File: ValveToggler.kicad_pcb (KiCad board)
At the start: 2 copper layers, 70 x 50 mm, 29 parts, among them J1 24V IN, J17 MODE, J2 Coil1, J3 Coil2, Q6 BC557, Q7 2N7000, Q8 BC557, Q9 2N7000, U1 NE555P, U2 NE555P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

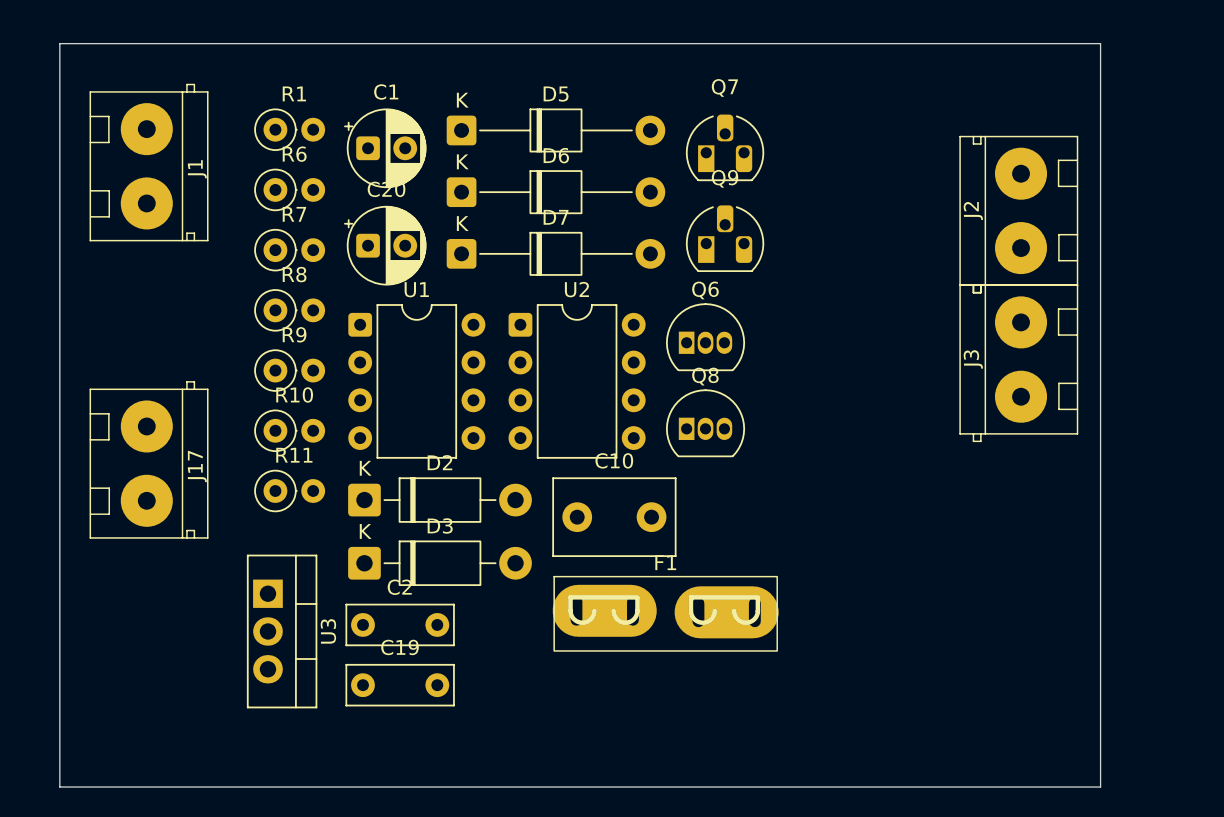
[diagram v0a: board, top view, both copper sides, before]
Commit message: Layout: Arrange footprints, start poc routing
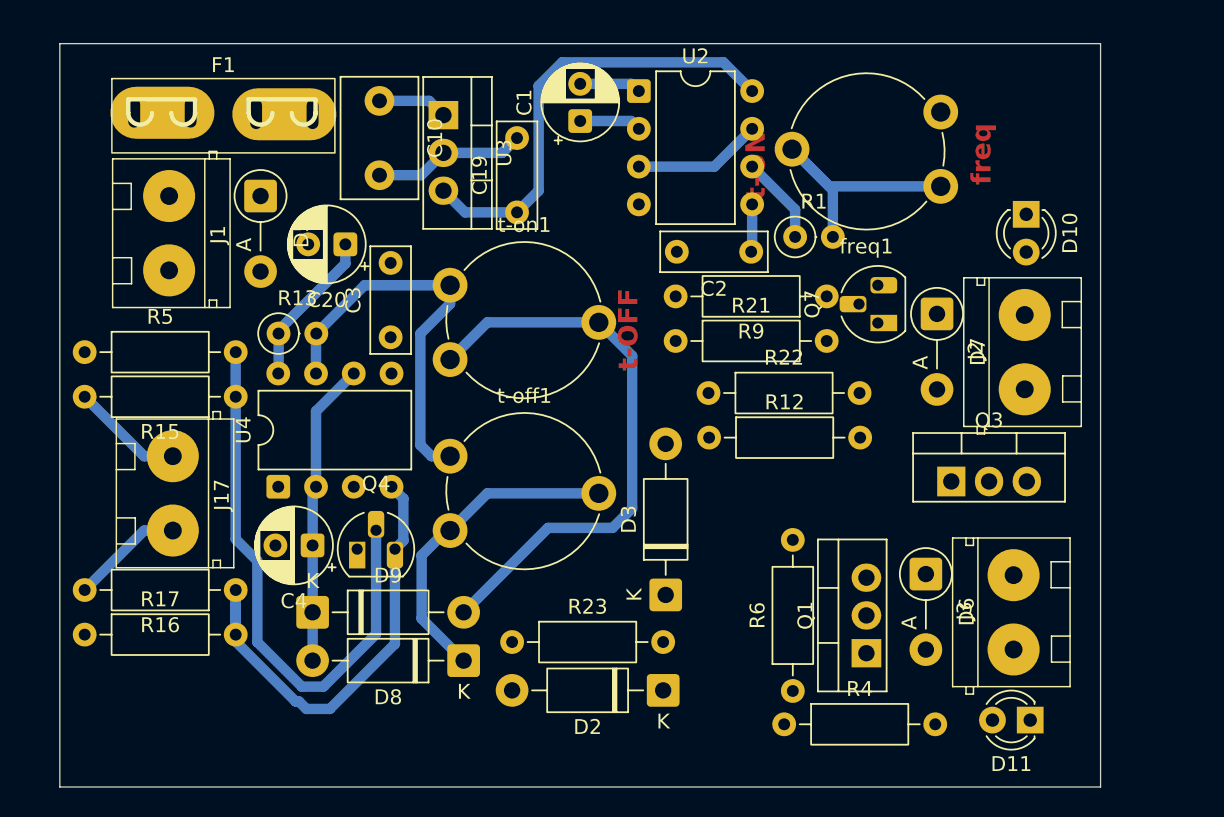
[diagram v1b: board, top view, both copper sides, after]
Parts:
- removed Q6, Q8: BC557, Package_TO_SOT_THT:TO-92_Inline
- removed Q9: 2N7000, Package_TO_SOT_THT:TO-92_HandSolder
- removed R10: 10k, Resistor_THT:R_Axial_DIN0207_L6.3mm_D2.5mm_P2.54mm_Vertical
- removed R11, R7, R8: 47k, Resistor_THT:R_Axial_DIN0207_L6.3mm_D2.5mm_P2.54mm_Vertical
- removed U1: NE555P, Package_DIP:DIP-8_W7.62mm
- added C3: 100nF, Capacitor_THT:C_Disc_D7.0mm_W2.5mm_P5.00mm, F.Cu at (67.2, 64.8)
- added C4: 47u, Capacitor_THT:CP_Radial_D5.0mm_P2.50mm, F.Cu at (62.0, 78.8)
- added D10: LED2_orange, LED_THT:LED_D3.0mm_Clear, F.Cu at (110.0, 56.5)
- added D11: LED1_green, LED_THT:LED_D3.0mm_Clear, F.Cu at (110.3, 90.5)
- added D8: 1N5817, Diode_THT:D_DO-41_SOD81_P10.16mm_Horizontal, F.Cu at (72.2, 86.5)
- added D9: 1N5817, Diode_THT:D_DO-41_SOD81_P10.16mm_Horizontal, F.Cu at (62.0, 83.2)
- added Q1: IRFZ24N, Package_TO_SOT_THT:TO-220-3_Vertical, F.Cu at (99.2, 86.0)
- added Q3: IRFZ24N, Package_TO_SOT_THT:TO-220-3_Vertical, F.Cu at (105.0, 74.5)
- added Q4: 2N7000, Package_TO_SOT_THT:TO-92_HandSolder, F.Cu at (65.0, 79.0)
- added R12: 1k5, Resistor_THT:R_Axial_DIN0207_L6.3mm_D2.5mm_P10.16mm_Horizontal, F.Cu at (88.7, 71.5)
- added R13: 1k5, Resistor_THT:R_Axial_DIN0207_L6.3mm_D2.5mm_P2.54mm_Vertical, F.Cu at (59.7, 64.5)
- added R15: 2k2, Resistor_THT:R_Axial_DIN0207_L6.3mm_D2.5mm_P10.16mm_Horizontal, F.Cu at (56.8, 68.8)
- added R16: 2k2, Resistor_THT:R_Axial_DIN0207_L6.3mm_D2.5mm_P10.16mm_Horizontal, F.Cu at (56.8, 81.8)
- added R17: 2k2, Resistor_THT:R_Axial_DIN0207_L6.3mm_D2.5mm_P10.16mm_Horizontal, F.Cu at (46.7, 84.8)
- added R21: 330, Resistor_THT:R_Axial_DIN0207_L6.3mm_D2.5mm_P10.16mm_Horizontal, F.Cu at (86.4, 65.0)
- added R22: 330, Resistor_THT:R_Axial_DIN0207_L6.3mm_D2.5mm_P10.16mm_Horizontal, F.Cu at (88.6, 68.5)
- added R23: 330, Resistor_THT:R_Axial_DIN0207_L6.3mm_D2.5mm_P10.16mm_Horizontal, F.Cu at (75.4, 85.2)
- added R4: 1k5, Resistor_THT:R_Axial_DIN0207_L6.3mm_D2.5mm_P10.16mm_Horizontal, F.Cu at (93.7, 90.8)
- added R5: 2k2, Resistor_THT:R_Axial_DIN0207_L6.3mm_D2.5mm_P10.16mm_Horizontal, F.Cu at (46.7, 65.8)
- added U4: NE555P, Package_DIP:DIP-8_W7.62mm, F.Cu at (59.7, 74.8)
- added freq1: 10k, Potentiometer_THT:Potentiometer_Piher_PT-10-V10_Vertical, F.Cu at (104.2, 49.6)
- added t-off1: 100k, Potentiometer_THT:Potentiometer_Piher_PT-10-V10_Vertical, F.Cu at (71.2, 77.8)
- added t-on1: 10k, Potentiometer_THT:Potentiometer_Piher_PT-10-V10_Vertical, F.Cu at (71.2, 66.2)
- D5, D6, D7: footprint Diode_THT:D_T-1_P12.70mm_Horizontal -> Diode_THT:D_DO-41_SOD81_P5.08mm_Vertical_AnodeUp
- J17: value MODE -> MODE (24V)
- J2: value Coil1 -> Coil2
- J3: value Coil2 -> Coil1
- R1: value 10k -> 1k5
- R6: value 47k -> 10k; footprint Resistor_THT:R_Axial_DIN0207_L6.3mm_D2.5mm_P2.54mm_Vertical -> Resistor_THT:R_Axial_DIN0207_L6.3mm_D2.5mm_P10.16mm_Horizontal
- R9: footprint Resistor_THT:R_Axial_DIN0207_L6.3mm_D2.5mm_P2.54mm_Vertical -> Resistor_THT:R_Axial_DIN0207_L6.3mm_D2.5mm_P10.16mm_Horizontal
- moved R6 48.4 mm to (94.3, 88.5), turned to 90 degrees
- moved F1 44.8 mm to (50.0, 49.8)
- moved D6 40.4 mm to (103.2, 80.7), turned to -90 degrees
- moved R9 37.4 mm to (96.6, 62.0), turned to 180 degrees
- moved C2 36.2 mm to (91.5, 59.0), turned to 180 degrees
- moved R1 35.7 mm to (94.5, 58.0)
- moved U3 34.3 mm to (70.8, 49.8)
- moved C19 33.4 mm to (75.8, 56.4), turned to 90 degrees
- moved D7 32.2 mm to (104.0, 63.2), turned to -90 degrees
- moved C10 31.0 mm to (66.5, 48.9), turned to -90 degrees
- moved D2 23.8 mm to (85.6, 88.5), turned to 180 degrees
- moved D3 20.4 mm to (85.8, 82.1), turned to 90 degrees
- moved U2 17.6 mm to (83.9, 48.2)
- moved J3 17.0 mm to (109.2, 85.8)
- moved Q7 16.3 mm to (100.0, 63.8), turned to 90 degrees
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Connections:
- net Net-(Q4-G) renamed /MOS2
- C10 pad 2: GNDPWR -> GND
- C19 pad 1: +5VA -> +12V
- C19 pad 2: GNDPWR -> GND
- C20 pad 1: +5VA -> +12V
- C20 pad 2: GNDPWR -> GND
- D2 pad 1: Net-(D2-K) -> /MOS1
- D2 pad 2: /F1 -> /F1_signal-mode1
- D3 pad 1: Net-(D2-K) -> /MOS1
- D3 pad 2: /F2 -> /F2_signal-mode2
- D5 pad 2: GNDPWR -> GND
- J1 pad 2: GNDPWR -> GND
- J17 pad 1: /MODE_SINGLE -> /MODE_DOUBLE_IN
- J17 pad 2: /MODE_DOUBLE -> /MODE_SINGLE_IN
- Q7 pad 2: /F2 -> Net-(Q7-G)
- R1 pad 2: /F2 -> Net-(R1-Pad2)
- R6 pad 1: Net-(D2-K) -> Net-(Q1-G)
- R6 pad 2: GNDPWR -> GND
- R9 pad 2: Net-(Q8-C) -> /MODE_DOUBLE_12V
- U2 pad 3: /F2 -> /F2_signal-mode2
- U2 pad 4: /MODE_DOUBLE -> /MODE_DOUBLE_12V
- U2 pad 7: /F2 -> /F2_signal-mode2
- U3 pad 2: GNDPWR -> GND
- U3 pad 3: +5VA -> +12V
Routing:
- net +12V: track 0.00 -> 41.0 mm
- net Net-(D9-A): track 0.00 -> 38.7 mm
- net /MODE_DOUBLE_12V: track 0.00 -> 37.8 mm
- net /MODE_SINGLE_12V: track 0.00 -> 32.0 mm
- net Net-(U4-DIS): track 0.00 -> 26.9 mm
- net Net-(D8-K): track 0.00 -> 21.9 mm
- net Net-(D8-A): track 0.00 -> 20.5 mm
- net Net-(R1-Pad2): track 0.00 -> 18.1 mm
- net GND: track 0.00 -> 14.4 mm
- net Net-(U2-THR): track 0.00 -> 10.1 mm
- net /F2_signal-mode2: track 0.00 -> 8.67 mm
- net /MODE_SINGLE_IN: track 0.00 -> 7.59 mm
- net /MODE_DOUBLE_IN: track 0.00 -> 7.59 mm
- net +24V: track 0.00 -> 4.70 mm
- net Net-(U2-CV): track 0.00 -> 3.22 mm
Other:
- copper layers 2 -> 4
- board text added: "M1 M2"
- board text added: "freq"
- board text added: "t-OFF"
- board text added: "t-ON"

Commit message: Routing complete, DRC pass
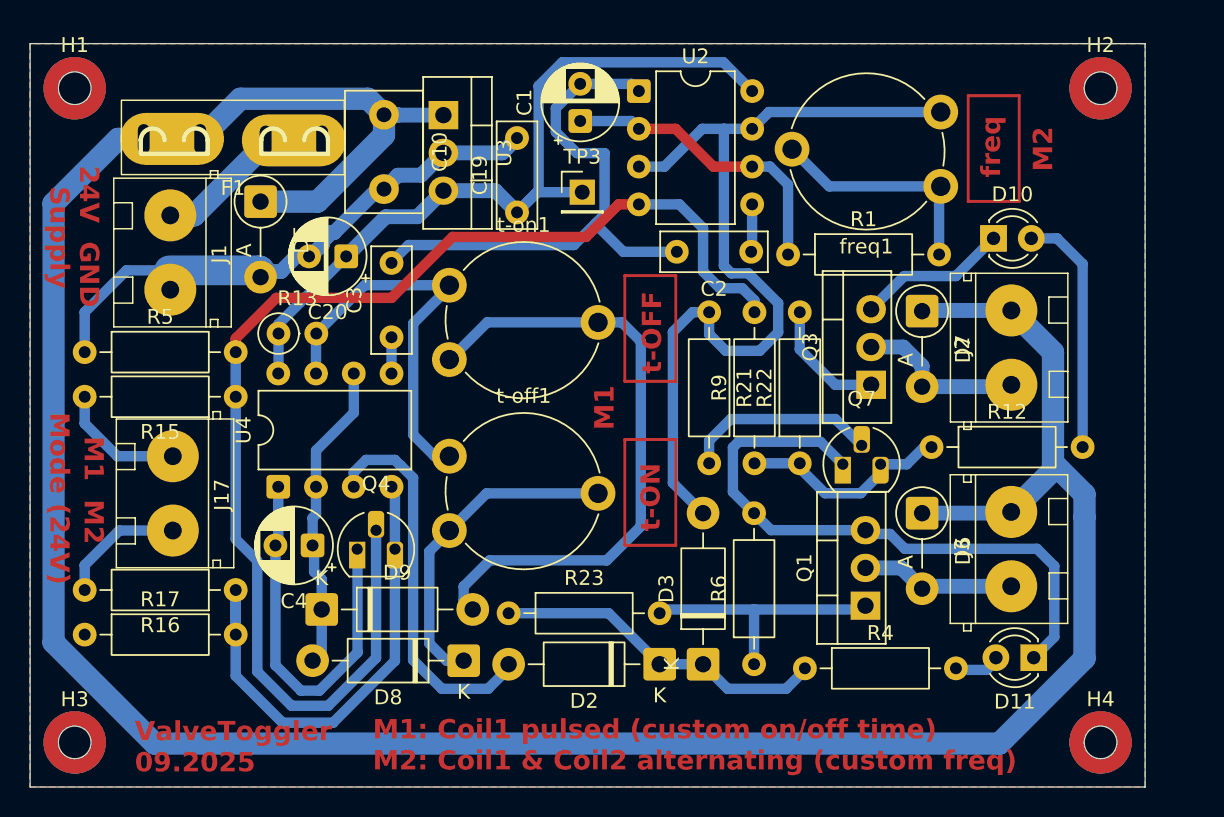
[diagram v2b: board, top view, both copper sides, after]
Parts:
- added H1: MountingHole_Pad, mountingHoles_libJonny:MountingHole_2.2mm_NPTH-with-pad_DRC-clearance-error, F.Cu at (46.0, 48.0)
- added H2: MountingHole_Pad, mountingHoles_libJonny:MountingHole_2.2mm_NPTH-with-pad_DRC-clearance-error, F.Cu at (115.0, 48.0)
- added H3: MountingHole_Pad, mountingHoles_libJonny:MountingHole_2.2mm_NPTH-with-pad_DRC-clearance-error, F.Cu at (46.0, 92.0)
- added H4: MountingHole_Pad, mountingHoles_libJonny:MountingHole_2.2mm_NPTH-with-pad_DRC-clearance-error, F.Cu at (115.0, 92.0)
- added TP3: 12V, Connector_PinHeader_2.54mm:PinHeader_1x01_P2.54mm_Vertical, F.Cu at (80.1, 55.0)
- R1: footprint Resistor_THT:R_Axial_DIN0207_L6.3mm_D2.5mm_P2.54mm_Vertical -> Resistor_THT:R_Axial_DIN0207_L6.3mm_D2.5mm_P10.16mm_Horizontal
- moved R12 15.0 mm to (103.6, 72.1)
- moved F1 12.8 mm to (62.6, 51.4), turned to 180 degrees
- moved R9 12.2 mm to (91.7, 73.2), turned to 90 degrees
- moved Q7 9.79 mm to (97.7, 73.3), turned to 0 degrees
- moved Q3 8.45 mm to (99.6, 67.9), turned to 90 degrees
- moved R22 7.75 mm to (94.8, 73.2), turned to 90 degrees
- moved D3 5.30 mm to (88.3, 86.7)
- moved J3 4.26 mm to (109.0, 81.5)
- moved D11 4.21 mm to (110.5, 86.3)
- moved D6 4.10 mm to (103.0, 76.6)
- moved R4 4.01 mm to (95.1, 87.0)
- moved Q1 3.20 mm to (99.2, 82.8)
- moved R6 3.17 mm to (91.7, 86.7)
- moved R21 2.97 mm to (88.7, 63.1), turned to -90 degrees
- moved D10 2.73 mm to (107.8, 58.1), turned to 0 degrees
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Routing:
- net +24V: track 4.70 -> 187.1 mm
- net GND: track 14.4 -> 153.1 mm
- net /F2_signal-mode2: track 8.67 -> 60.8 mm
- net /MODE_DOUBLE_12V: track 37.8 -> 85.7 mm
- net /F1_signal-mode1: track 0.00 -> 26.1 mm
- net /MOS1: track 0.00 -> 22.7 mm
- net Net-(Q1-G): track 0.00 -> 17.7 mm
- net Net-(D10-A): track 0.00 -> 16.5 mm
- net /MOS2: track 0.00 -> 14.6 mm
- net Net-(Q7-G): track 0.00 -> 13.1 mm
- net +12V: track 41.0 -> 53.6 mm
- net Net-(J1-Pin_1): track 0.00 -> 12.3 mm
- net Net-(D7-A): track 0.00 -> 11.4 mm
- net Net-(D6-A): track 0.00 -> 10.4 mm
- net Net-(U2-THR): track 10.1 -> 20.5 mm
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- added copper zone on B.Cu, net GND
- added copper zone on F.Cu, net GND
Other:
- board size 70 x 50 mm -> 75 x 50 mm
- board text added: "- +"
- board text added: "24V GND"
- board text added: "Coil1"
- board text added: "Coil2"
- board text added: "IN:"
- board text added: "M1"
- board text added: "M1: Coil1 pulsed (custom on/off time) M2: Coil1 & Coil2 alternating (custom freq)"
- board text added: "M2"
- board text added: "Mode (24V)"
- board text added: "OUT:"
- board text added: "Supply"
- board text added: "ValveToggler 09.2025"

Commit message: Add R to trimmer (offMin), rework routing, Add timing calculation notes
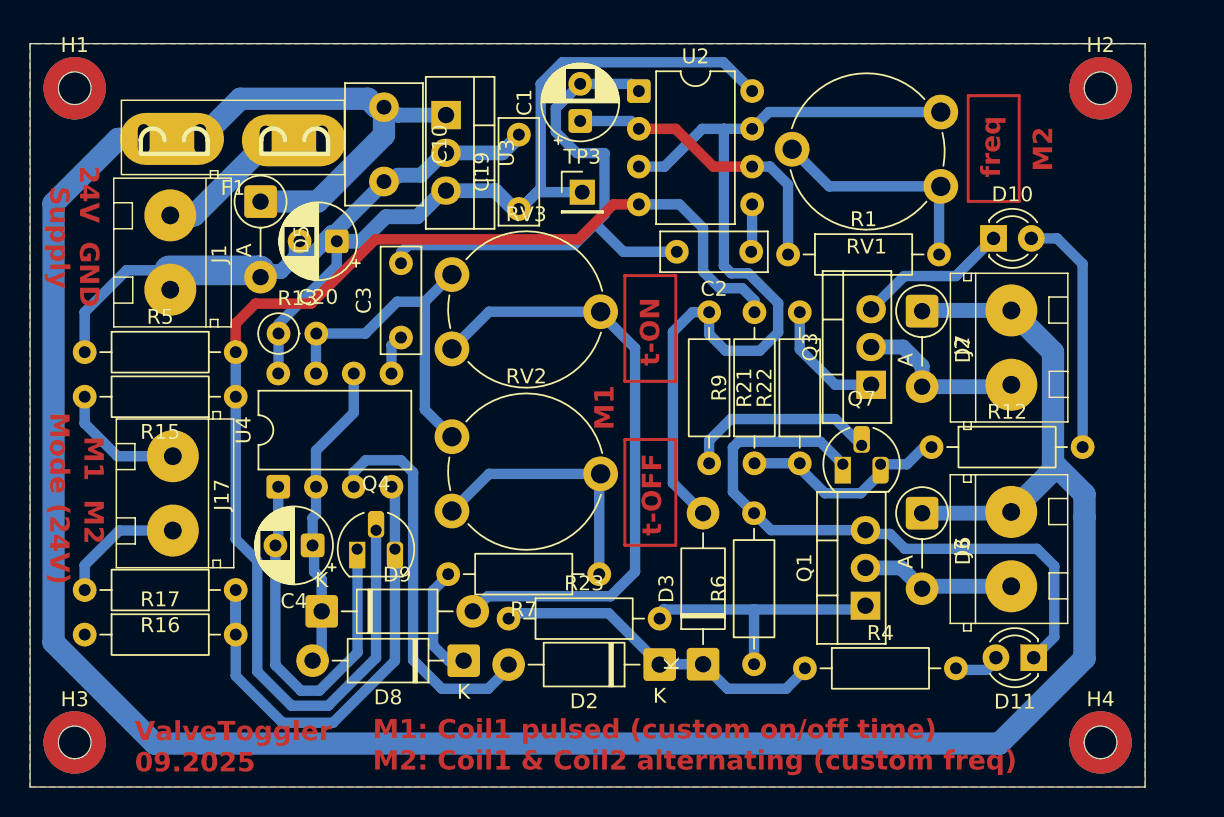
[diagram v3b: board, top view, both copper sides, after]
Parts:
- removed freq1, t-on1: 10k, Potentiometer_THT:Potentiometer_Piher_PT-10-V10_Vertical
- removed t-off1: 100k, Potentiometer_THT:Potentiometer_Piher_PT-10-V10_Vertical
- added R7: 3k3_t-offMin, Resistor_THT:R_Axial_DIN0207_L6.3mm_D2.5mm_P10.16mm_Horizontal, F.Cu at (81.3, 80.7)
- added RV1: 50k_freq1, resistors_libJonny:Potentiometer_Piher_PT-10-V10_Vertical, F.Cu at (104.3, 49.6)
- added RV2: 100k_t-off, resistors_libJonny:Potentiometer_Piher_PT-10-V10_Vertical, F.Cu at (71.4, 76.4)
- added RV3: 50k_t-on, resistors_libJonny:Potentiometer_Piher_PT-10-V10_Vertical, F.Cu at (71.4, 65.5)
- R1: value 1k5 -> 1k5_f-min
- R13: value 1k5 -> 1k5_t-onMin
- moved C20 1.20 mm to (63.6, 58.3)
- moved C3 0.64 mm to (67.9, 64.8)
- moved C10 0.51 mm to (66.8, 49.3)
- moved R23 0.36 mm to (75.2, 83.7)
- moved C19 0.26 mm to (75.9, 56.1)
- moved U3 0.18 mm to (71.0, 49.8)
- moved D9 0.13 mm to (62.6, 83.2)
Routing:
- net Net-(R7-Pad1): track 0.00 -> 18.7 mm
- net Net-(D8-K): track 22.0 -> 7.69 mm
- net Net-(U4-DIS): track 27.1 -> 23.3 mm
- net GND: track 153.1 -> 154.5 mm
- net Net-(D9-A): track 42.3 -> 41.5 mm
- net +24V: track 187.1 -> 187.8 mm
- net /MODE_DOUBLE_12V: track 85.7 -> 86.3 mm

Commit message: Final adjustments pre milling: Mounthole, Text layer, Text thickness
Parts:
- added H5: MountingHole_Pad, mountingHoles_libJonny:MountingHole_2.2mm_NPTH-with-pad_DRC-clearance-error, F.Cu at (76.4, 68.3)
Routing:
- net GND: track 154.5 -> 154.0 mm

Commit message: Arrange Fab text, Update actually soldered Values, Add milled gerber export
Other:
- board text added: "Layer User7: Marked pads to solder on top side"
